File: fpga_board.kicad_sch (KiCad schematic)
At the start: 131 parts, among them J2 Conn_01x06, J3 USB_C_Receptacle, Q1 2N7002PW, Q2 2N7002PW, Q3 2N7002PW, SW1 SW_Push, U1 LFE5U-45F-7BG256I, U10 TLV62569DRL, U2 CYUSB3014-BZXC, U5 K4B4G1646E-BCMA, U6 K4B4G1646E-BCMA, U7 TLV62569DRL, U8 TLV62569DRL, U9 TLV62569DRL, X1 XO32, Y1 Crystal_GND24

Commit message: added capacitor and resistor footprints
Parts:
- C1, C10, C11, C12, C13, C14, C15, C16, C17, C18, C19, C2, C20, C21, C22, C23, C24, C25, C26, C29, C3, C31, C33, C35, C37, C38, C39, C40, C41, C42, C43, C44, C45, C46, C47, C48, C49, C50, C51, C52, C53, C54, C55, C57, C58, C59, C6, C60, C61, C8, C9: footprint (none) -> Capacitor_SMD:C_0402_1005Metric
- C30, C32, C34, C36, C4, C5, C7: footprint (none) -> Capacitor_SMD:C_0603_1608Metric
- R1, R17, R18, R19, R2, R23, R25, R26, R27, R28, R29, R3, R30, R31, R32, R33, R34, R35, R39, R4, R40, R5, R6, R7, R8: footprint (none) -> Resistor_SMD:R_0402_1005Metric
- R10, R11, R12, R13, R14, R15, R16, R20, R21, R22, R24, R37, R38, R9: footprint (none) -> Resistor_SMD:R_0603_1608Metric
- R36: value 60 -> 62; footprint (none) -> Resistor_SMD:R_0402_1005Metric

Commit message: added RGB LED for FPGA, added termintaion to FPGA crystal
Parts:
- removed C58: 10pF, Capacitor_SMD:C_0402_1005Metric, symbol Device:C
- added D1: LED_RGBA, LED_SMD:LED_Wurth_150044M155260, symbol Device:LED_RGBA
- added Q4, Q5, Q6: 2N7002PW, Package_TO_SOT_SMD:SOT-323_SC-70, symbol Simulation_SPICE:NMOS
- added R41, R42, R43: 10k, Resistor_SMD:R_0402_1005Metric, symbol Device:R
- added R44: 62, Resistor_SMD:R_0402_1005Metric, symbol Device:R
- added R45, R46, R47: 20, Resistor_SMD:R_0402_1005Metric, symbol Device:R
- L1, L2, L3, L4: footprint (none) -> Inductor_SMD:L_0603_1608Metric
- L5, L6, L7, L8: footprint (none) -> Inductor:IND_VLS3015_TDK
- Q1, Q2, Q3: footprint (none) -> Package_TO_SOT_SMD:SOT-323_SC-70
- TP1, TP2, TP3, TP4, TP5: footprint (none) -> TestPoint:TestPoint_Pad_D1.5mm
- TP6: renamed from TP9; footprint (none) -> TestPoint:TestPoint_Pad_D1.5mm
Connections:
- net VCCIO8 is gone; now on net 3v3: J2.2 (Pin_2), R17.1, R23.2, R25.2, R28.2, R40.2
- net 3v3: now also D1.2 (A)
- net FPGA_CLK: now also R47.2; no longer X1.3 (OUT)
- net GND: now also Q4.3 (S), Q5.3 (S), Q6.3 (S), R41.2, R42.2, R43.2
- net FPGA.R: now reaches U1.D10 (PT56A)
- net FPGA.R: now also Q4.2 (G), R41.1
- net FPGA.B: now reaches U1.D11 (PT69A)
- net FPGA.B: now also Q6.2 (G), R43.1
- net FPGA.G: now reaches U1.E10 (PT56B)
- net FPGA.G: now also Q5.2 (G), R42.1
- new net: Q4.1 (D), R44.1
- new net: Q5.1 (D), R45.1
- new net: D1.4 (GK), R45.2
- new net: Q6.1 (D), R46.1
- new net: R47.1, X1.3 (OUT)
- new net: D1.1 (RK), R44.2
- new net: D1.3 (BK), R46.2

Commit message: update to kicad 9.0.6 and other changes
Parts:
- added C56: 0.1µF, Capacitor_SMD:C_0402_1005Metric, symbol Device:C
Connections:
- net GND: now also C56.1
- net RESET#: now also C56.2

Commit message: finished schematic, finished BOM.
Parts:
- removed J2: Conn_01x06, symbol Connector_Generic:Conn_01x06
- removed J3: USB_C_Receptacle, symbol Connector:USB_C_Receptacle
- removed SW1: SW_Push, symbol Switch:SW_Push
- added H1: PH2.54-2X3P-H25, PIN-HEADER:HDR-TH_6P-P2.54-V-M-R2-C3-S2.54-1, symbol PIN-HEADER:PH2.54-2X3P-H25
- added SW1: 1TS028A-1300-0600-CT, BUTTON:SW-SMD_4P-L2.8-W1.9-P1.20-LS3.0_1TS028A, symbol BUTTON:1TS028A-1300-0600-CT
- added USB1: TYPE-C 24P QT 143, USB-TYPE-C:TYPE-C-SMD_C9900025773, symbol USB-TYPE-C:TYPE-C24PQT143
- TP1, TP2, TP3, TP4, TP5, TP6: footprint TestPoint:TestPoint_Pad_D1.5mm -> TestPoint:TestPoint_Pad_D1.0mm
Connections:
- net 3v3: now also H1.2
- net 5v_VBUS: now also USB1.A4 (VBUS), USB1.A9 (VBUS), USB1.B4 (VBUS), USB1.B9 (VBUS)
- net D_N: now also USB1.A7 (DN1)
- net D_P: now also USB1.A6 (DP1)
- net GND: now also H1.1, SW1.2, SW1.4, USB1.A1 (GND), USB1.A12 (GND), USB1.B1 (GND), USB1.B12 (GND)
- net JTAG.TCK: now also H1.4
- net JTAG.TDI: now also H1.3
- net JTAG.TDO: now also H1.5
- net JTAG.TMS: now also H1.6
- net RESET#: now also SW1.1, SW1.3
- net SS_RX_M: now also USB1.A10 (SSRXn2)
- net SS_RX_P: now also USB1.A11 (SSRXp2)
- net SS_TX_M: now also USB1.A3 (SSTXn1)
- net SS_TX_P: now also USB1.A2 (SSTXP1)
- net at C61.1, R38.1: now also USB1.15 (EP), USB1.16 (EP), USB1.17 (EP), USB1.18 (EP)
- net at R39.1: now also USB1.A5 (CC1)
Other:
- moved on the sheet: C61, R29, R38, R39, TP6

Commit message: added pre-commit for schematic svg generation, edited readme, organized schematic.
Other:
- note added: "DDR3_Memory"
- note added: "FPGA"
- note added: "FPGA_RGB_LED"
- note added: "FX3_RGB_LED"
- note added: "Power"
- note added: "Reset_switch"
- note added: "USB"
- moved on the sheet: C1, C10, C11, C12, C13, C14, C15, C16, C17, C18, C19, C2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

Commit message: layout: buck converters placed
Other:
- moved on the sheet: C35, C36, L8, R15, R16, TP4, U10

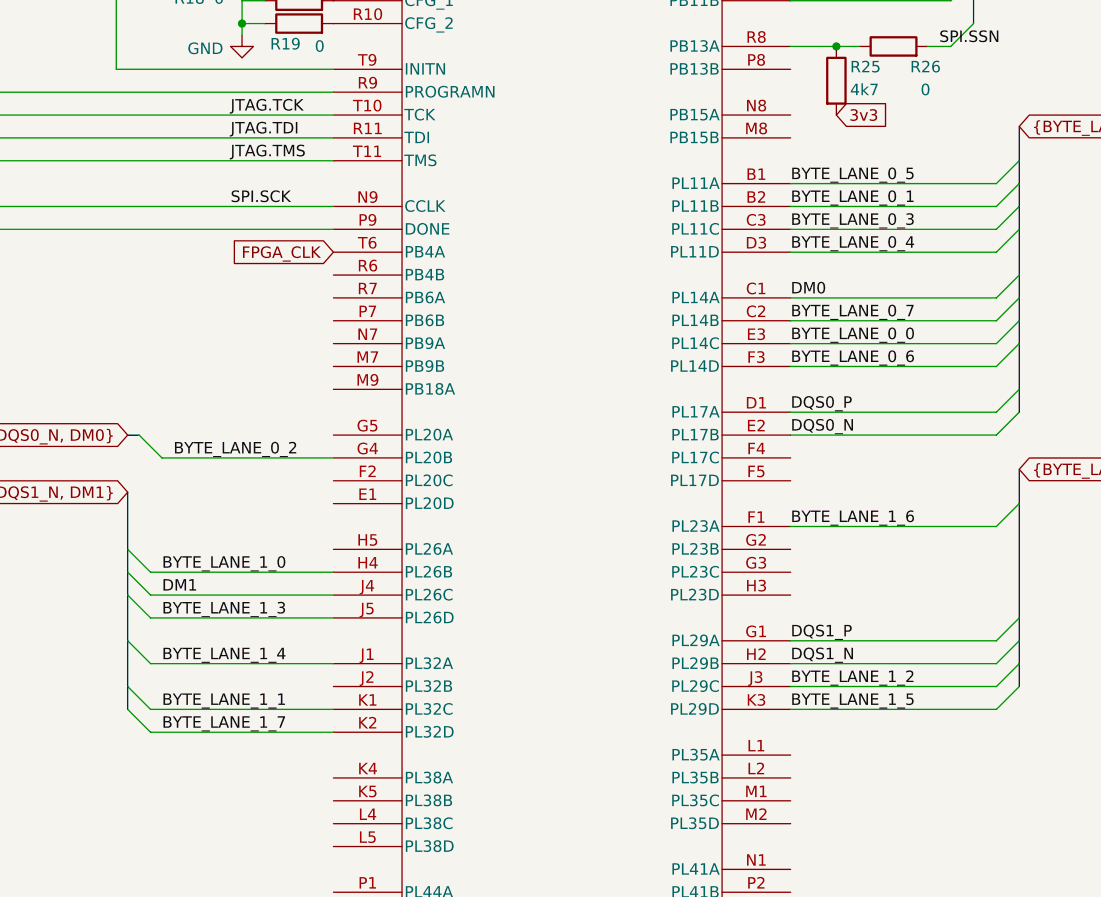
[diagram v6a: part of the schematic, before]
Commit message: BYTE_LANE 0 and 1 routed and length matched to DDR memory
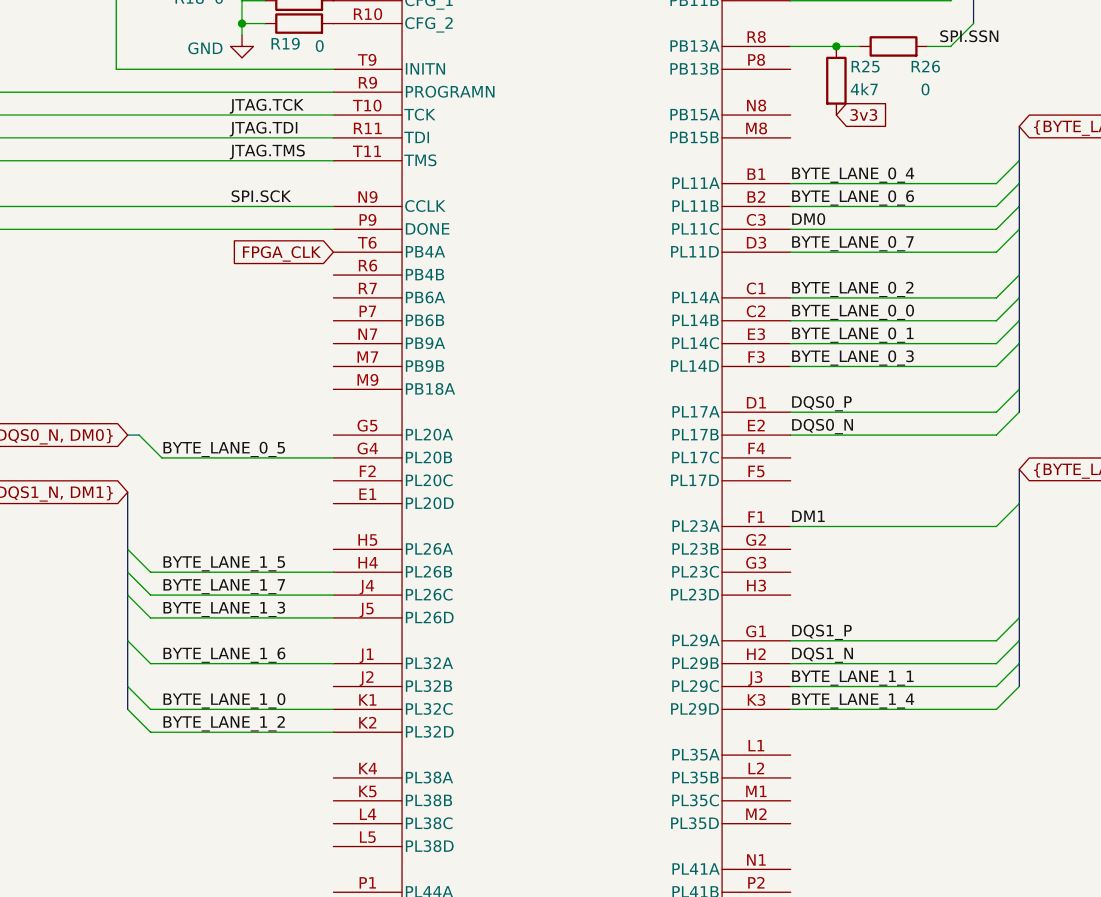
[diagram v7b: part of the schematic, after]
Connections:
- net BYTE_LANE_0_0: now also U1.C2 (PL14B); no longer U1.E3 (PL14C)
- net BYTE_LANE_0_1: now also U1.E3 (PL14C); no longer U1.B2 (PL11B)
- net BYTE_LANE_0_2: now also U1.C1 (PL14A); no longer U1.G4 (PL20B)
- net BYTE_LANE_0_3: now also U1.F3 (PL14D); no longer U1.C3 (PL11C)
- net BYTE_LANE_0_4: now also U1.B1 (PL11A); no longer U1.D3 (PL11D)
- net BYTE_LANE_0_5: now also U1.G4 (PL20B); no longer U1.B1 (PL11A)
- net BYTE_LANE_0_6: now also U1.B2 (PL11B); no longer U1.F3 (PL14D)
- net BYTE_LANE_0_7: now also U1.D3 (PL11D); no longer U1.C2 (PL14B)
- net BYTE_LANE_1_0: now also U1.K1 (PL32C); no longer U1.H4 (PL26B)
- net BYTE_LANE_1_1: now also U1.J3 (PL29C); no longer U1.K1 (PL32C)
- net BYTE_LANE_1_2: now also U1.K2 (PL32D); no longer U1.J3 (PL29C)
- net BYTE_LANE_1_4: now also U1.K3 (PL29D); no longer U1.J1 (PL32A)
- net BYTE_LANE_1_5: now also U1.H4 (PL26B); no longer U1.K3 (PL29D)
- net BYTE_LANE_1_6: now also U1.J1 (PL32A); no longer U1.F1 (PL23A)
- net BYTE_LANE_1_7: now also U1.J4 (PL26C); no longer U1.K2 (PL32D)
- net DM0: now also U1.C3 (PL11C); no longer U1.C1 (PL14A)
- net DM1: now also U1.F1 (PL23A); no longer U1.J4 (PL26C)
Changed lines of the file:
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@@
 	)
 	(label "BYTE_LANE_0_6"
-		(at 199.39 478.79 0)
+		(at 199.39 461.01 0)
 		(effects
 			(font
@@
 	)
 	(label "BYTE_LANE_0_4"
-		(at 199.39 466.09 0)
+		(at 199.39 458.47 0)
 		(effects
 			(font
@@
 	)
 	(label "BYTE_LANE_0_3"
-		(at 199.39 463.55 0)
+		(at 199.39 478.79 0)
 		(effects
 			(font
@@
 	)
 	(label "BYTE_LANE_0_0"
-		(at 199.39 476.25 0)
+		(at 199.39 473.71 0)
 		(effects
 			(font
@@
 	)
 	(label "DM1"
-		(at 129.54 504.19 0)
+		(at 199.39 496.57 0)
 		(effects
 			(font
@@
 	)
 	(label "BYTE_LANE_1_7"
-		(at 129.54 519.43 0)
+		(at 129.54 504.19 0)
 		(effects
 			(font
@@
 	)
 	(label "BYTE_LANE_0_5"
-		(at 199.39 458.47 0)
+		(at 129.54 488.95 0)
 		(effects
 			(font
@@
 	)
 	(label "BYTE_LANE_1_2"
-		(at 199.39 514.35 0)
+		(at 129.54 519.43 0)
 		(effects
 			(font
@@
 	)
 	(label "BYTE_LANE_0_1"
-		(at 199.39 461.01 0)
+		(at 199.39 476.25 0)
 		(effects
 			(font
@@
 	)
 	(label "BYTE_LANE_0_2"
-		(at 130.81 488.95 0)
+		(at 199.39 471.17 0)
 		(effects
 			(font
@@
 	)
 	(label "BYTE_LANE_0_7"
-		(at 199.39 473.71 0)
+		(at 199.39 466.09 0)
 		(effects
 			(font
@@
 	)
 	(label "BYTE_LANE_1_6"
-		(at 199.39 496.57 0)
+		(at 129.54 511.81 0)
 		(effects
 			(font
@@
 	)
 	(label "BYTE_LANE_1_5"
-		(at 199.39 516.89 0)
+		(at 129.54 501.65 0)
 		(effects
 			(font
@@
 	)
 	(label "BYTE_LANE_1_0"
-		(at 129.54 501.65 0)
+		(at 129.54 516.89 0)
 		(effects
 			(font
@@
 	)
 	(label "DM0"
-		(at 199.39 471.17 0)
+		(at 199.39 463.55 0)
 		(effects
 			(font
@@
 	)
 	(label "BYTE_LANE_1_1"
-		(at 129.54 516.89 0)
+		(at 199.39 514.35 0)
 		(effects
 			(font
@@
 	)
 	(label "BYTE_LANE_1_4"
-		(at 129.54 511.81 0)
-		(effects
-			(font
+		(at 199.39 516.89 0)
+		(effects
+			(font

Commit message: all DDR byte lanes routed and length matched
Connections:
- net BYTE_LANE_2_0: now also U1.M1 (PL35C)
- net BYTE_LANE_2_1: now also U1.R1 (PL44B)
- net BYTE_LANE_2_2: now also U1.L2 (PL35B)
- net BYTE_LANE_2_3: now also U1.M3 (PL41D)
- net BYTE_LANE_2_4: now also U1.K4 (PL38A)
- net BYTE_LANE_2_5: now also U1.N3 (PL44D)
- net BYTE_LANE_2_6: now also U1.L1 (PL35A)
- net BYTE_LANE_2_7: now also U1.P1 (PL44A)
- net BYTE_LANE_3_0: now also U1.P6 (PL68C)
- net BYTE_LANE_3_1: now also U1.R2 (PL59C)
- net BYTE_LANE_3_2: now also U1.T2 (PL59D)
- net BYTE_LANE_3_3: now also U1.P4 (PL62A)
- net BYTE_LANE_3_4: now also U1.M6 (PL68A)
- net BYTE_LANE_3_5: now also U1.P3 (PL59B)
- net BYTE_LANE_3_6: now also U1.N6 (PL68B)
- net BYTE_LANE_3_7: now also U1.P5 (PL68D)
- net DM2: now also U1.M2 (PL35D)
- net DM3: now also U1.N4 (PL59A)
- net DQS2_N: now also U1.P2 (PL41B)
- net DQS2_P: now also U1.N1 (PL41A)
- net DQS3_N: now also U1.T4 (PL65B)
- net DQS3_P: now also U1.R5 (PL65A)
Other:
- moved on the sheet: D1, Q4, Q5, Q6, R41, R42, R43, R44, R45, R46
